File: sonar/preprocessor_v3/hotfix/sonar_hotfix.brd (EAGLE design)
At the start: 37.1 x 15.2 mm, 9 parts

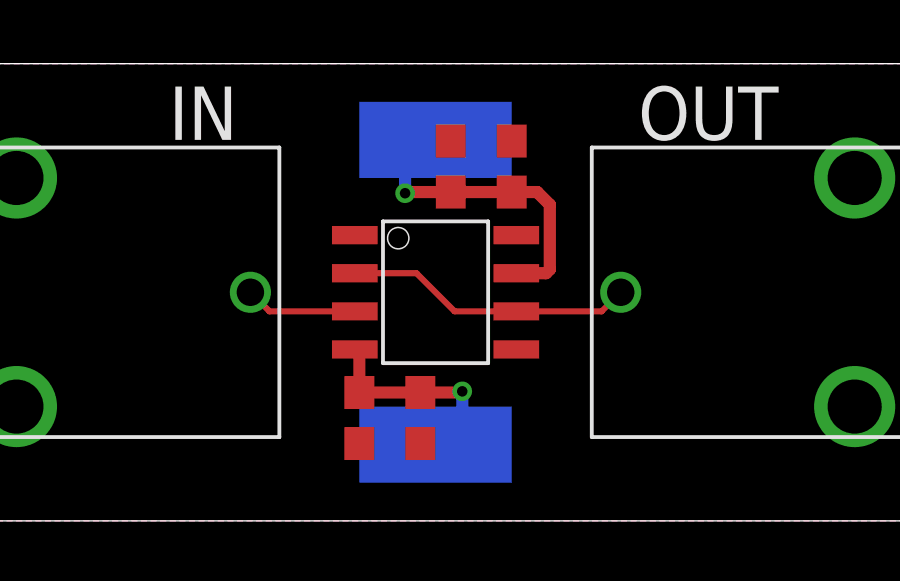
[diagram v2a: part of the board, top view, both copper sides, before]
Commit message: Added CAM files; Changed power trace layout; Renamed test pads
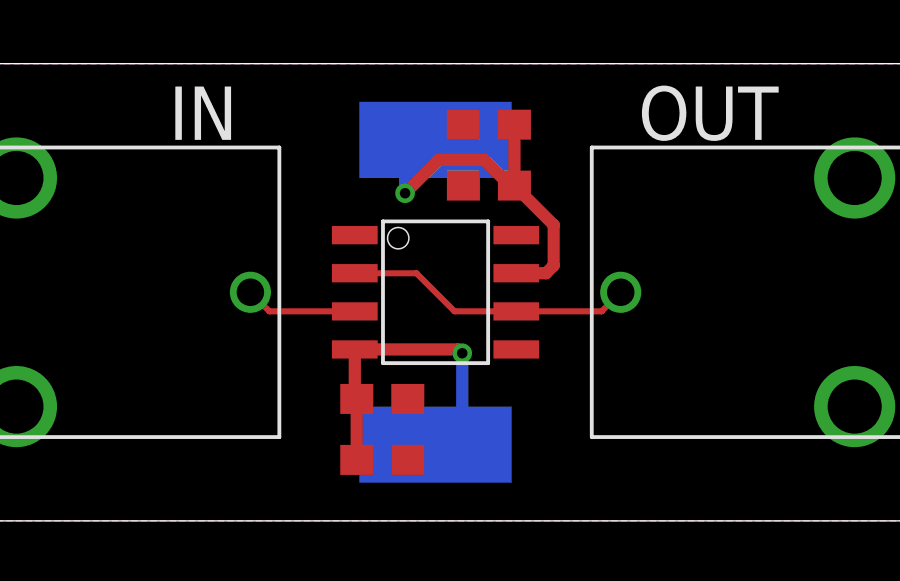
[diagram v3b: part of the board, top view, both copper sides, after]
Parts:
- moved C2 1.59 mm to (21.1, 2.03), turned to 0 degrees
- moved C3 1.59 mm to (24.6, 13.2), turned to 180 degrees
- moved C4 1.42 mm to (24.6, 11.2), turned to 180 degrees
- moved C1 1.42 mm to (21.1, 4.06), turned to 0 degrees
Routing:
- net -5V: track 7.09 -> 10.8 mm
- net +5V: track 10.5 -> 13.3 mm
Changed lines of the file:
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@@
 <element name="PAD1" library="wirepad" library_urn="urn:adsk.eagle:library:412" package="5-2,5" package3d_urn="urn:adsk.eagle:package:30845/1" value="WIREPADSMD5-2,5" x="22.86" y="12.7" smashed="yes" rot="MR90"/>
 <element name="PAD2" library="wirepad" library_urn="urn:adsk.eagle:library:412" package="5-2,5" package3d_urn="urn:adsk.eagle:package:30845/1" value="WIREPADSMD5-2,5" x="22.86" y="2.54" smashed="yes" rot="MR90"/>
-<element name="C1" library="rcl" library_urn="urn:adsk.eagle:library:334" package="C0603" package3d_urn="urn:adsk.eagle:package:23616/2" value="" x="22.352" y="3.429" smashed="yes" rot="R270">
-<attribute name="SPICEPREFIX" value="C" x="22.352" y="3.429" size="1.778" layer="27" rot="R270" display="off"/>
-<attribute name="VALUE" x="20.447" y="4.064" size="1.27" layer="27" rot="R270"/>
+<element name="C1" library="rcl" library_urn="urn:adsk.eagle:library:334" package="C0603" package3d_urn="urn:adsk.eagle:package:23616/2" value="" x="21.082" y="4.064" smashed="yes">
+<attribute name="SPICEPREFIX" value="C" x="21.082" y="4.064" size="1.778" layer="27" display="off"/>
+<attribute name="VALUE" x="20.447" y="2.159" size="1.27" layer="27"/>
 </element>
-<element name="C2" library="rcl" library_urn="urn:adsk.eagle:library:334" package="C0603" package3d_urn="urn:adsk.eagle:package:23616/2" value="" x="20.32" y="3.429" smashed="yes" rot="R270">
-<attribute name="SPICEPREFIX" value="C" x="20.32" y="3.429" size="1.778" layer="27" rot="R270" display="off"/>
-<attribute name="VALUE" x="18.415" y="4.064" size="1.27" layer="27" rot="R270"/>
+<element name="C2" library="rcl" library_urn="urn:adsk.eagle:library:334" package="C0603" package3d_urn="urn:adsk.eagle:package:23616/2" value="" x="21.082" y="2.032" smashed="yes">
+<attribute name="SPICEPREFIX" value="C" x="21.082" y="2.032" size="1.778" layer="27" display="off"/>
+<attribute name="VALUE" x="20.447" y="0.127" size="1.27" layer="27"/>
 </element>
-<element name="C3" library="rcl" library_urn="urn:adsk.eagle:library:334" package="C0603" package3d_urn="urn:adsk.eagle:package:23616/2" value="" x="25.4" y="11.811" smashed="yes" rot="R90">
-<attribute name="SPICEPREFIX" value="C" x="25.4" y="11.811" size="1.778" layer="27" rot="R90" display="off"/>
-<attribute name="VALUE" x="27.305" y="11.176" size="1.27" layer="27" rot="R90"/>
+<element name="C3" library="rcl" library_urn="urn:adsk.eagle:library:334" package="C0603" package3d_urn="urn:adsk.eagle:package:23616/2" value="" x="24.638" y="13.208" smashed="yes" rot="R180">
+<attribute name="SPICEPREFIX" value="C" x="24.638" y="13.208" size="1.778" layer="27" rot="R180" display="off"/>
+<attribute name="VALUE" x="25.273" y="15.113" size="1.27" layer="27" rot="R180"/>
 </element>
-<element name="C4" library="rcl" library_urn="urn:adsk.eagle:library:334" package="C0603" package3d_urn="urn:adsk.eagle:package:23616/2" value="" x="23.368" y="11.811" smashed="yes" rot="R90">
-<attribute name="SPICEPREFIX" value="C" x="23.368" y="11.811" size="1.778" layer="27" rot="R90" display="off"/>
-<attribute name="VALUE" x="25.273" y="11.176" size="1.27" layer="27" rot="R90"/>
+<element name="C4" library="rcl" library_urn="urn:adsk.eagle:library:334" package="C0603" package3d_urn="urn:adsk.eagle:package:23616/2" value="" x="24.638" y="11.176" smashed="yes" rot="R180">
+<attribute name="SPICEPREFIX" value="C" x="24.638" y="11.176" size="1.778" layer="27" rot="R180" display="off"/>
+<attribute name="VALUE" x="25.273" y="13.081" size="1.27" layer="27" rot="R180"/>
 </element>
 </elements>
@@
 <contactref element="C3" pad="1"/>
 <contactref element="C4" pad="1"/>
-<wire x1="23.368" y1="10.961" x2="25.4" y2="10.961" width="0.4064" layer="1"/>
-<wire x1="25.4" y1="10.961" x2="26.25" y2="10.961" width="0.4064" layer="1"/>
-<wire x1="26.25" y1="10.961" x2="26.67" y2="10.541" width="0.4064" layer="1"/>
-<wire x1="26.67" y1="8.382" x2="26.543" y2="8.255" width="0.4064" layer="1"/>
-<wire x1="26.543" y1="8.255" x2="25.5524" y2="8.255" width="0.4064" layer="1"/>
-<wire x1="26.67" y1="10.541" x2="26.67" y2="8.382" width="0.4064" layer="1"/>
-<wire x1="23.368" y1="10.961" x2="21.883" y2="10.961" width="0.4064" layer="1"/>
 <wire x1="21.883" y1="10.961" x2="21.844" y2="10.922" width="0.4064" layer="1"/>
 <via x="21.844" y="10.922" extent="1-16" drill="0.35"/>
 <wire x1="21.844" y1="10.922" x2="21.844" y2="11.684" width="0.4064" layer="16"/>
 <wire x1="21.844" y1="11.684" x2="22.86" y2="12.7" width="0.4064" layer="16"/>
+<wire x1="25.5524" y1="8.255" x2="26.543" y2="8.255" width="0.4064" layer="1"/>
+<wire x1="26.543" y1="8.255" x2="26.797" y2="8.509" width="0.4064" layer="1"/>
+<wire x1="26.797" y1="9.867" x2="25.488" y2="11.176" width="0.4064" layer="1"/>
+<wire x1="26.797" y1="8.509" x2="26.797" y2="9.867" width="0.4064" layer="1"/>
+<wire x1="25.488" y1="11.176" x2="25.488" y2="13.208" width="0.4064" layer="1"/>
+<wire x1="25.34089375" y1="11.176" x2="25.488" y2="11.176" width="0.4064" layer="1"/>
+<wire x1="24.48529375" y1="12.0316" x2="25.34089375" y2="11.176" width="0.4064" layer="1"/>
+<wire x1="22.9536" y1="12.0316" x2="24.48529375" y2="12.0316" width="0.4064" layer="1"/>
+<wire x1="21.844" y1="10.922" x2="22.9536" y2="12.0316" width="0.4064" layer="1"/>
 </signal>
 <signal name="-5V">
@@
 <contactref element="C2" pad="1"/>
 <contactref element="C1" pad="1"/>
-<wire x1="22.352" y1="4.279" x2="20.32" y2="4.279" width="0.4064" layer="1"/>
-<wire x1="20.32" y1="4.279" x2="20.32" y2="5.5626" width="0.4064" layer="1"/>
-<wire x1="20.32" y1="5.5626" x2="20.1676" y2="5.715" width="0.4064" layer="1"/>
-<wire x1="22.352" y1="4.279" x2="23.71" y2="4.279" width="0.4064" layer="1"/>
-<wire x1="23.71" y1="4.279" x2="23.749" y2="4.318" width="0.4064" layer="1"/>
-<via x="23.749" y="4.318" extent="1-16" drill="0.35"/>
-<wire x1="23.749" y1="4.318" x2="23.749" y2="3.429" width="0.4064" layer="16"/>
+<via x="23.749" y="5.588" extent="1-16" drill="0.35"/>
+<wire x1="23.749" y1="5.588" x2="23.749" y2="3.429" width="0.4064" layer="16"/>
 <wire x1="23.749" y1="3.429" x2="22.86" y2="2.54" width="0.4064" layer="16"/>
+<wire x1="20.1676" y1="5.715" x2="20.1676" y2="4.1284" width="0.4064" layer="1"/>
+<wire x1="20.1676" y1="4.1284" x2="20.232" y2="4.064" width="0.4064" layer="1"/>
+<wire x1="20.232" y1="4.064" x2="20.232" y2="2.032" width="0.4064" layer="1"/>
+<wire x1="20.1676" y1="5.715" x2="23.622" y2="5.715" width="0.4064" layer="1"/>
+<wire x1="23.622" y1="5.715" x2="23.749" y2="5.588" width="0.4064" layer="1"/>
 </signal>
 <signal name="GND">
